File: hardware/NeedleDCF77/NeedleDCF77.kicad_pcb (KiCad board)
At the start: 2 copper layers, 3 parts, among them J1 USB_C_Receptacle_USB2.0, U1 LTC3558, U2 STM32L051C8Tx

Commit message: Import changes to PCB
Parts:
- added C1: 100nF, Capacitor_SMD:C_0805_2012Metric_Pad1.18x1.45mm_HandSolder, F.Cu at (233.5, 96.0)
- added C10: 22pF, Capacitor_SMD:C_0805_2012Metric_Pad1.18x1.45mm_HandSolder, F.Cu at (233.5, 108.0)
- added C11: 22pF, Capacitor_SMD:C_0805_2012Metric_Pad1.18x1.45mm_HandSolder, F.Cu at (238.3, 96.0)
- added C12: 10pF, Capacitor_SMD:C_0805_2012Metric_Pad1.18x1.45mm_HandSolder, F.Cu at (238.3, 99.0)
- added C13: 10pF, Capacitor_SMD:C_0805_2012Metric_Pad1.18x1.45mm_HandSolder, F.Cu at (238.3, 102.0)
- added C14: 10uF, Capacitor_Tantalum_SMD:CP_EIA-3216-18_Kemet-A_Pad1.58x1.35mm_HandSolder, F.Cu at (195.7, 111.4)
- added C15: 10pF, Capacitor_SMD:C_0805_2012Metric_Pad1.18x1.45mm_HandSolder, F.Cu at (238.3, 105.0)
- added C16: 4.7uF, Capacitor_SMD:CP_Elec_4x5.7, F.Cu at (249.4, 97.4)
- added C17: 10pF, Capacitor_SMD:C_0805_2012Metric_Pad1.18x1.45mm_HandSolder, F.Cu at (238.3, 108.0)
- added C18: 10pF, Capacitor_SMD:C_0805_2012Metric_Pad1.18x1.45mm_HandSolder, F.Cu at (243.1, 96.0)
- added C19: 100nF, Capacitor_SMD:C_0805_2012Metric_Pad1.18x1.45mm_HandSolder, F.Cu at (243.1, 99.0)
- added C2: 10uF, Capacitor_SMD:C_1206_3216Metric_Pad1.33x1.80mm_HandSolder, F.Cu at (251.4, 88.3)
- added C20: 4.7uF, Capacitor_Tantalum_SMD:CP_EIA-3528-21_Kemet-B_Pad1.50x2.35mm_HandSolder, F.Cu at (195.9, 115.1)
- added C21: 4.7uF, Capacitor_SMD:CP_Elec_4x5.7, F.Cu at (249.4, 103.3)
- added C22: 4.7uF, Capacitor_SMD:CP_Elec_4x5.7, F.Cu at (249.4, 109.1)
- added C23: 1uF, Capacitor_SMD:C_0805_2012Metric_Pad1.18x1.45mm_HandSolder, F.Cu at (243.1, 102.0)
- added C24: 100nF, Capacitor_SMD:C_0805_2012Metric_Pad1.18x1.45mm_HandSolder, F.Cu at (243.1, 105.0)
- added C3: 0.22uF, Capacitor_SMD:C_1206_3216Metric_Pad1.33x1.80mm_HandSolder, F.Cu at (251.4, 91.7)
- added C4: 10uF, Capacitor_Tantalum_SMD:CP_EIA-3216-18_Kemet-A_Pad1.58x1.35mm_HandSolder, F.Cu at (195.7, 101.9)
- added C5: 100nF, Capacitor_SMD:C_0805_2012Metric_Pad1.18x1.45mm_HandSolder, F.Cu at (233.5, 99.0)
- added C6: 100nF, Capacitor_SMD:C_0805_2012Metric_Pad1.18x1.45mm_HandSolder, F.Cu at (233.5, 102.0)
- added C7: 10uF, Capacitor_Tantalum_SMD:CP_EIA-3216-18_Kemet-A_Pad1.58x1.35mm_HandSolder, F.Cu at (195.7, 105.1)
- added C8: 10pF, Capacitor_SMD:C_0805_2012Metric_Pad1.18x1.45mm_HandSolder, F.Cu at (233.5, 105.0)
- added C9: 10uF, Capacitor_Tantalum_SMD:CP_EIA-3216-18_Kemet-A_Pad1.58x1.35mm_HandSolder, F.Cu at (195.7, 108.2)
- added D1: SSL14, Diode_SMD:D_SMA_Handsoldering, F.Cu at (241.9, 80.4)
- added D2: BZV55B5V6, Diode_SMD:D_MiniMELF, F.Cu at (240.2, 117.7)
- added D3: CD4148W, Diode_SMD:D_0805_2012Metric, F.Cu at (228.3, 115.2)
- added D4: 6.2V, Diode_THT:D_DO-35_SOD27_P2.54mm_Vertical_AnodeUp, F.Cu at (238.8, 84.5)
- added F1: 2A, Fuse:Fuse_2512_6332Metric_Pad1.52x3.35mm_HandSolder, F.Cu at (250.0, 114.5)
- added J2: Battery, Connector_Molex:Molex_KK-254_AE-6410-03A_1x03_P2.54mm_Vertical, F.Cu at (229.5, 82.0)
- added J3: DSW, Connector_PinHeader_2.54mm:PinHeader_1x04_P2.54mm_Vertical, F.Cu at (255.6, 96.8)
- added J4: UART, Connector_PinHeader_2.54mm:PinHeader_1x03_P2.54mm_Vertical, F.Cu at (217.6, 106.7)
- added J5: Hours, Connector_Molex:Molex_KK-254_AE-6410-02A_1x02_P2.54mm_Vertical, F.Cu at (222.2, 90.6)
- added J6: Minutes, Connector_Molex:Molex_KK-254_AE-6410-02A_1x02_P2.54mm_Vertical, F.Cu at (229.3, 90.6)
- added J7: Seconds, Connector_Molex:Molex_KK-254_AE-6410-02A_1x02_P2.54mm_Vertical, F.Cu at (236.5, 90.6)
- added JP1: ~, Jumper:SolderJumper-2_P1.3mm_Open_TrianglePad1.0x1.5mm, F.Cu at (245.1, 84.4)
- added L1: 15uH, Inductor_SMD:L_12x12mm_H8mm, F.Cu at (193.5, 79.0)
- added L2: 15uH, Inductor_SMD:L_12x12mm_H8mm, F.Cu at (193.5, 93.2)
- added L3: 4.7uH, Inductor_SMD:L_Ferrocore_DLG-0504, F.Cu at (252.4, 75.4)
- added L4: 2.2uH, Inductor_SMD:L_Ferrocore_DLG-0504, F.Cu at (252.4, 82.4)
- added R1: 5k1, Resistor_SMD:R_0805_2012Metric_Pad1.20x1.40mm_HandSolder, F.Cu at (203.3, 88.1)
- added R10: 120k, Resistor_SMD:R_1206_3216Metric_Pad1.30x1.75mm_HandSolder, F.Cu at (234.0, 111.2)
- added R11: 300k, Resistor_SMD:R_0805_2012Metric_Pad1.20x1.40mm_HandSolder, F.Cu at (208.0, 97.0)
- added R12: 1, Resistor_SMD:R_0805_2012Metric_Pad1.20x1.40mm_HandSolder, F.Cu at (208.0, 99.9)
- added R13: 820k, Resistor_SMD:R_0805_2012Metric_Pad1.20x1.40mm_HandSolder, F.Cu at (208.0, 102.9)
- added R14: 62k, Resistor_THT:R_Axial_DIN0207_L6.3mm_D2.5mm_P2.54mm_Vertical, F.Cu at (221.9, 115.7)
- added R15: 15k, Resistor_SMD:R_0805_2012Metric_Pad1.20x1.40mm_HandSolder, F.Cu at (212.8, 88.1)
- added R16: 390k, Resistor_SMD:R_0805_2012Metric_Pad1.20x1.40mm_HandSolder, F.Cu at (212.8, 91.1)
- added R17: 10k, Resistor_SMD:R_0805_2012Metric_Pad1.20x1.40mm_HandSolder, F.Cu at (212.8, 94.0)
- added R18: 10k, Resistor_SMD:R_0805_2012Metric_Pad1.20x1.40mm_HandSolder, F.Cu at (212.8, 97.0)
- added R19: 22k, Resistor_SMD:R_0805_2012Metric_Pad1.20x1.40mm_HandSolder, F.Cu at (212.8, 99.9)
- added R2: 5k1, Resistor_SMD:R_0805_2012Metric_Pad1.20x1.40mm_HandSolder, F.Cu at (203.3, 91.1)
- added R20: R_Small, Resistor_SMD:R_0805_2012Metric_Pad1.20x1.40mm_HandSolder, F.Cu at (212.8, 102.9)
- added R21: R_Small, Resistor_SMD:R_0805_2012Metric_Pad1.20x1.40mm_HandSolder, F.Cu at (217.5, 88.1)
- added R22: R_Small, Resistor_SMD:R_0805_2012Metric_Pad1.20x1.40mm_HandSolder, F.Cu at (217.5, 91.1)
- added R23: 51k, Resistor_SMD:R_0603_1608Metric_Pad0.98x0.95mm_HandSolder, F.Cu at (228.2, 118.0)
- added R24: 3R9, Resistor_SMD:R_1206_3216Metric_Pad1.30x1.75mm_HandSolder, F.Cu at (234.0, 114.5)
- added R25: 470, Resistor_SMD:R_0805_2012Metric_Pad1.20x1.40mm_HandSolder, F.Cu at (217.5, 94.0)
- added R26: 470, Resistor_SMD:R_0805_2012Metric_Pad1.20x1.40mm_HandSolder, F.Cu at (217.5, 97.0)
- added R27: 3R9, Resistor_SMD:R_1206_3216Metric_Pad1.30x1.75mm_HandSolder, F.Cu at (234.0, 117.8)
- added R3: Rntc, Resistor_SMD:R_0805_2012Metric_Pad1.20x1.40mm_HandSolder, F.Cu at (203.3, 94.0)
- added R4: 100k, Resistor_SMD:R_0805_2012Metric_Pad1.20x1.40mm_HandSolder, F.Cu at (203.3, 97.0)
- added R5: 820k, Resistor_SMD:R_0805_2012Metric_Pad1.20x1.40mm_HandSolder, F.Cu at (203.3, 99.9)
- added R6: 1k8, Resistor_SMD:R_0805_2012Metric_Pad1.20x1.40mm_HandSolder, F.Cu at (203.3, 102.9)
- added R7: 300k, Resistor_SMD:R_0805_2012Metric_Pad1.20x1.40mm_HandSolder, F.Cu at (208.0, 88.1)
- added R8: 100k, Resistor_SMD:R_0805_2012Metric_Pad1.20x1.40mm_HandSolder, F.Cu at (208.0, 91.1)
- added R9: 1k, Resistor_SMD:R_0805_2012Metric_Pad1.20x1.40mm_HandSolder, F.Cu at (208.0, 94.0)
- added RV1: Hour_pot, Potentiometer_THT:Potentiometer_Bourns_3296Y_Vertical, F.Cu at (228.0, 96.4)
- added RV2: Minutes_pot, Potentiometer_THT:Potentiometer_Bourns_3296Y_Vertical, F.Cu at (228.0, 102.8)
- added RV3: Second_pot, Potentiometer_THT:Potentiometer_Bourns_3296Y_Vertical, F.Cu at (228.0, 109.2)
- added SW1: ShowDate, Connector_Molex:Molex_KK-254_AE-6410-02A_1x02_P2.54mm_Vertical, F.Cu at (243.6, 90.6)
- added U3: MAS6180_77kHz, DCF77_module:MAS6180_module, F.Cu at (201.7, 72.6)
- added U4: LT1617, Package_TO_SOT_SMD:SOT-23-5_HandSoldering, F.Cu at (189.0, 115.8)
- added U5: PT6312, Package_QFP:LQFP-44_10x10mm_P0.8mm, F.Cu at (208.1, 111.5)
- added U6: LM4871, Package_SO:SOIC-8_3.9x4.9mm_P1.27mm, F.Cu at (241.2, 112.8)
- added VFD1: FG95A, VFD:FG95A, F.Cu at (194.3, 70.1)
- added Y1: 8MHz, Crystal:Crystal_SMD_HC49-SD_HandSoldering, F.Cu at (237.9, 75.0)
- added Y2: 32.768kHz, Crystal:Crystal_C38-LF_D3.0mm_L8.0mm_Horizontal_1EP_style2, F.Cu at (188.5, 101.7)
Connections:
- J1 pad A1: Net-(J1-PadA1) -> GND
- J1 pad A12: Net-(J1-PadA1) -> GND
- J1 pad A5: unconnected-(J1-PadA5) -> Net-(J1-CC1)
- J1 pad B1: Net-(J1-PadA1) -> GND
- J1 pad B12: Net-(J1-PadA1) -> GND
- J1 pad B5: unconnected-(J1-PadB5) -> Net-(J1-CC2)
- J1 pad S1: unconnected-(J1-PadS1) -> GND
- U1 pad 1: unconnected-(U1-Pad1) -> GND
- U1 pad 10: unconnected-(U1-Pad10) -> Net-(U1-SWCD2)
- U1 pad 11: unconnected-(U1-Pad11) -> +5VD
- U1 pad 12: unconnected-(U1-Pad12) -> LTC_SUSP
- U1 pad 13: unconnected-(U1-Pad13) -> Net-(U1-FB2)
- U1 pad 14: unconnected-(U1-Pad14) -> Net-(U1-Vc2)
- U1 pad 15: unconnected-(U1-Pad15) -> Net-(U1-EN2)
- U1 pad 16: unconnected-(U1-Pad16) -> LTC_HPWR
- U1 pad 17: unconnected-(U1-Pad17) -> NTC
- U1 pad 18: unconnected-(U1-Pad18) -> Net-(U1-PROG)
- U1 pad 19: unconnected-(U1-Pad19) -> LTC_CHRG
- U1 pad 2: unconnected-(U1-Pad2) -> VBAT
- U1 pad 20: unconnected-(U1-Pad20) -> VBUS_P
- U1 pad 21: unconnected-(U1-Pad21) -> GND
- U1 pad 3: unconnected-(U1-Pad3) -> LTC_MODE
- U1 pad 4: unconnected-(U1-Pad4) -> Net-(U1-FB1)
- U1 pad 5: unconnected-(U1-Pad5) -> Net-(U1-EN1)
- U1 pad 6: unconnected-(U1-Pad6) -> Net-(U1-SW1)
- U1 pad 7: unconnected-(U1-Pad7) -> VBAT
- U1 pad 8: unconnected-(U1-Pad8) -> VBAT
- U1 pad 9: unconnected-(U1-Pad9) -> Net-(U1-SWAB2)
- U2 pad 10: unconnected-(U2-Pad10) -> GPIO_EXTI0
- U2 pad 11: unconnected-(U2-Pad11) -> PWM_Min
- U2 pad 12: unconnected-(U2-Pad12) -> PWM_Hour
- U2 pad 13: unconnected-(U2-Pad13) -> PWM_Sec
- U2 pad 14: unconnected-(U2-Pad14) -> SPI1_NSS
- U2 pad 15: unconnected-(U2-Pad15) -> PWM_Fosc
- U2 pad 16: unconnected-(U2-Pad16) -> DCF77_TIME
- U2 pad 21: unconnected-(U2-Pad21) -> DCF77_PDN
- U2 pad 22: unconnected-(U2-Pad22) -> ~{SHDN_-24V}
- U2 pad 23: unconnected-(U2-Pad23) -> GND
- U2 pad 24: unconnected-(U2-Pad24) -> +3V0
- U2 pad 25: unconnected-(U2-Pad25) -> LTC_SUSP
- U2 pad 26: unconnected-(U2-Pad26) -> LTC_HPWR
- U2 pad 27: unconnected-(U2-Pad27) -> LTC_MODE
- U2 pad 28: unconnected-(U2-Pad28) -> LTC_CHRG
- U2 pad 3: unconnected-(U2-Pad3) -> Net-(U2-PC14)
- U2 pad 30: unconnected-(U2-Pad30) -> USART1_TX
- U2 pad 31: unconnected-(U2-Pad31) -> USART1_RX
- U2 pad 34: unconnected-(U2-Pad34) -> SWDIO
- U2 pad 35: unconnected-(U2-Pad35) -> GND
- U2 pad 36: unconnected-(U2-Pad36) -> +3V0
- U2 pad 37: unconnected-(U2-Pad37) -> SWCLK
- U2 pad 39: unconnected-(U2-Pad39) -> SPI1_SCK
- U2 pad 4: unconnected-(U2-Pad4) -> Net-(U2-PC15)
- U2 pad 40: unconnected-(U2-Pad40) -> SPI1_MISO
- U2 pad 41: unconnected-(U2-Pad41) -> SPI1_MOSI
- U2 pad 47: unconnected-(U2-Pad47) -> GND
- U2 pad 48: unconnected-(U2-Pad48) -> +3V0
- U2 pad 5: unconnected-(U2-Pad5) -> Net-(U2-PH0)
- U2 pad 6: unconnected-(U2-Pad6) -> Net-(U2-PH1)
- U2 pad 7: unconnected-(U2-Pad7) -> Net-(U2-NRST)
- U2 pad 8: unconnected-(U2-Pad8) -> GND
- U2 pad 9: unconnected-(U2-Pad9) -> +3V0

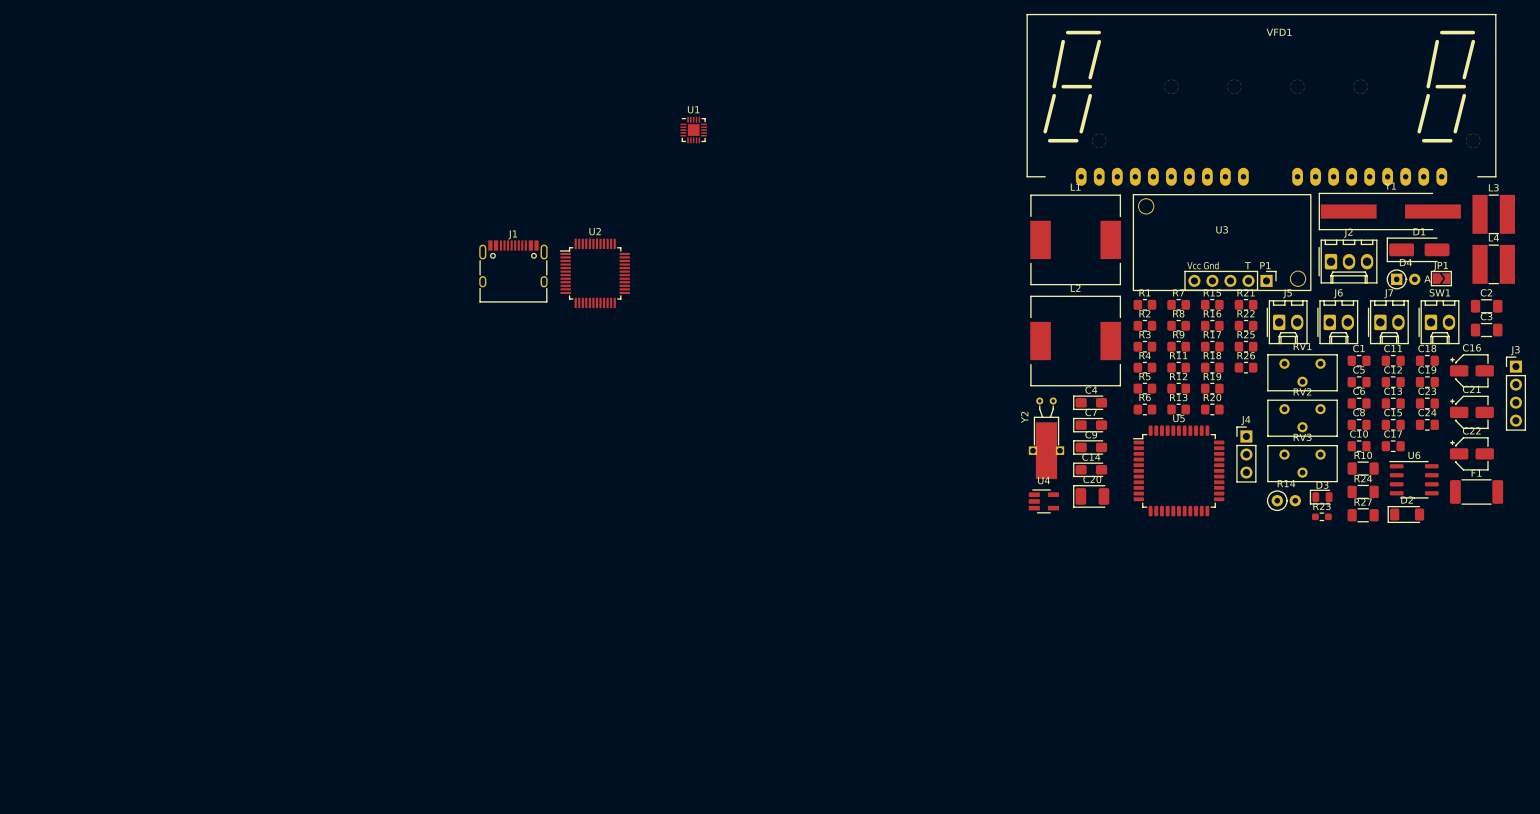
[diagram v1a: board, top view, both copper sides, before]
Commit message: Add battery measurement circuit and generate ADC code
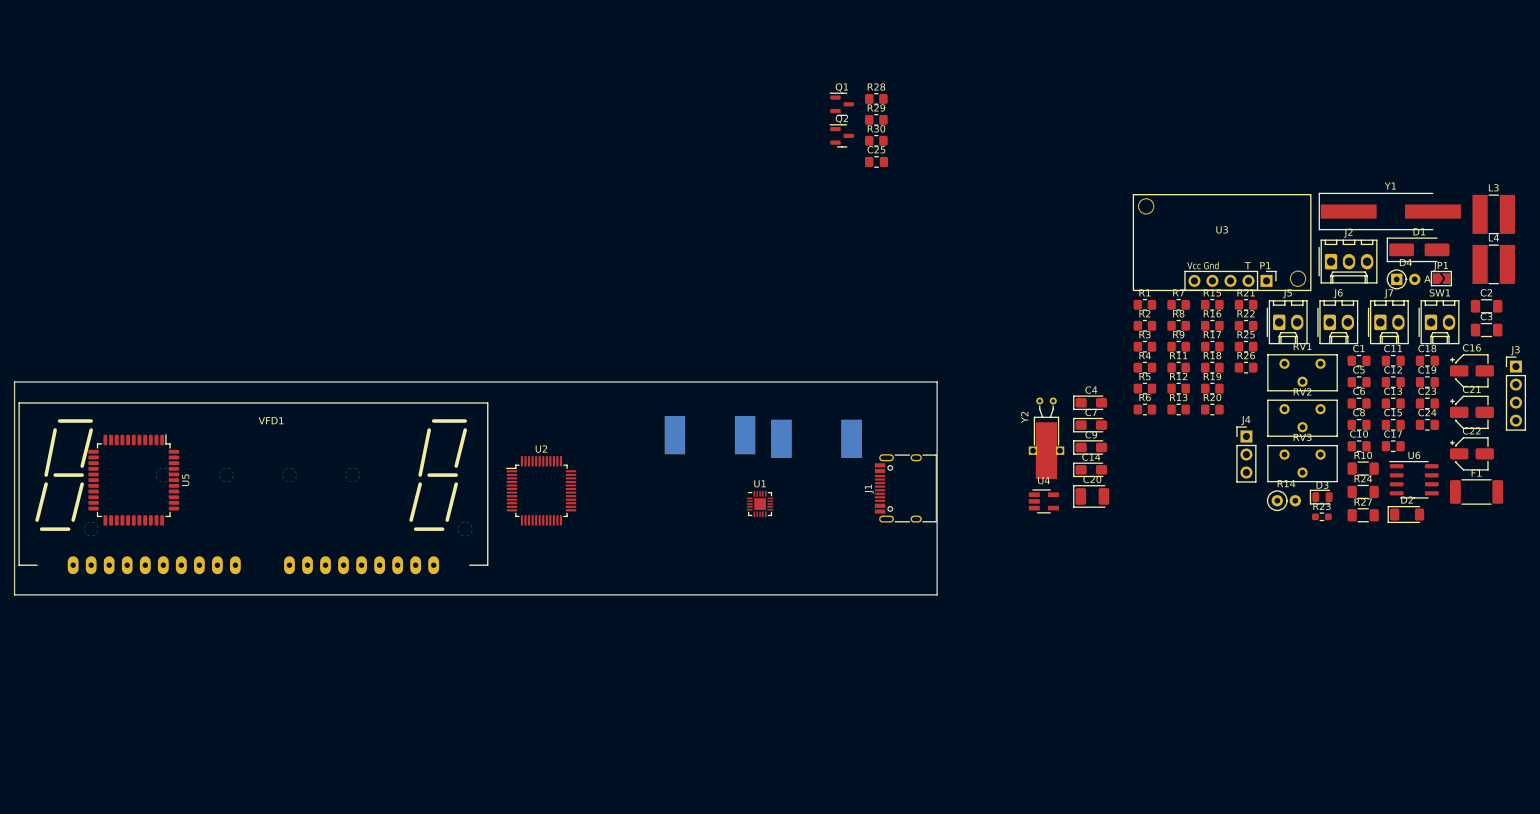
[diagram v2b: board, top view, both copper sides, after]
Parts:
- added C25: 10pF, Capacitor_SMD:C_0805_2012Metric_Pad1.18x1.45mm_HandSolder, F.Cu at (165.5, 68.0)
- added Q1: AO3401A, Package_TO_SOT_SMD:SOT-23, F.Cu at (160.6, 59.9)
- added Q2: AO3400A, Package_TO_SOT_SMD:SOT-23, F.Cu at (160.6, 64.3)
- added R28: 100k, Resistor_SMD:R_0805_2012Metric_Pad1.20x1.40mm_HandSolder, F.Cu at (165.4, 59.1)
- added R29: 22k, Resistor_SMD:R_0805_2012Metric_Pad1.20x1.40mm_HandSolder, F.Cu at (165.4, 62.1)
- added R30: 22k, Resistor_SMD:R_0805_2012Metric_Pad1.20x1.40mm_HandSolder, F.Cu at (165.4, 65.0)
- L1, L2: moved to B.Cu
- moved VFD1 152.2 mm to (52.3, 124.8)
- moved U5 147.3 mm to (60.8, 112.8), turned to -90 degrees
- moved J1 63.4 mm to (170.0, 114.0), turned to 90 degrees
- moved L1 58.4 mm to (142.0, 106.5), turned to 180 degrees
- moved U1 53.5 mm to (149.1, 116.2)
- moved L2 39.0 mm to (157.0, 107.0), turned to 180 degrees
- moved U2 31.6 mm to (118.2, 114.3)
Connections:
- U2 pad 17: unconnected-(U2-PA7-Pad17) -> BATT_LEVEL
- U2 pad 29: unconnected-(U2-PA8-Pad29) -> BATT_CHECK
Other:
- board outline added: 130 x 30 mm

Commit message: Bulk work - working on layout
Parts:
- C21, C22, J2, J3, J4, J5, J6, J7, L3, L4, SW1, Y1: moved to B.Cu
- R20: value R_Small -> 22k
- R21, R22: value R_Small -> 51k; footprint Resistor_SMD:R_0805_2012Metric_Pad1.20x1.40mm_HandSolder -> Resistor_SMD:R_0603_1608Metric_Pad0.98x0.95mm_HandSolder
- RV1: value Hour_pot -> 10k; moved to B.Cu
- RV2: value Minutes_pot -> 10k; moved to B.Cu
- RV3: value Second_pot -> 10k; moved to B.Cu
- moved C23 195.6 mm to (47.5, 104.4), turned to 90 degrees
- moved C22 194.3 mm to (55.2, 102.4)
- moved C21 194.2 mm to (55.2, 107.4)
- moved U6 188.4 mm to (53.0, 104.9)
- moved R24 182.6 mm to (51.5, 120.5), turned to -90 degrees
- moved C24 175.9 mm to (68.0, 121.5)
- moved D4 175.6 mm to (64.0, 101.4), turned to -90 degrees
- moved J4 171.2 mm to (52.5, 152.0), turned to 180 degrees
- moved C3 168.3 mm to (83.4, 102.0), turned to 180 degrees
- moved D1 167.3 mm to (76.0, 102.0)
- moved C2 164.9 mm to (87.5, 106.5), turned to -90 degrees
- moved R25 158.0 mm to (60.0, 106.9), turned to 90 degrees
- moved R26 157.6 mm to (60.0, 102.9), turned to -90 degrees
- moved R23 149.5 mm to (79.0, 108.5), turned to 180 degrees
- moved R27 142.3 mm to (92.5, 132.5)
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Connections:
- U2 pad 32: unconnected-(U2-PA11-Pad32) -> LTC_EN2
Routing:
- net GND: track 0.00 -> 8.65 mm
- net +5VD: track 0.00 -> 7.42 mm
- net Net-(U1-SWCD2): track 0.00 -> 7.00 mm, vias 0 -> 1
- net Net-(U6-+IN): track 0.00 -> 4.34 mm
- net Net-(C22-Pad2): track 0.00 -> 3.21 mm, vias 0 -> 1
- net Net-(C21-Pad2): track 0.00 -> 3.21 mm, vias 0 -> 1
- net Net-(U1-FB2): track 0.00 -> 2.97 mm
- net Net-(U1-EN2): track 0.00 -> 2.72 mm
- net Net-(U1-EN1): track 0.00 -> 2.46 mm
- net VBAT: track 0.00 -> 2.37 mm, vias 0 -> 1
- net Net-(U6-VO2): track 0.00 -> 2.32 mm, vias 0 -> 1
- net Net-(U6-VO1): track 0.00 -> 2.32 mm, vias 0 -> 1
- net Net-(U1-SWAB2): track 0.00 -> 2.21 mm, vias 0 -> 1
- net Net-(D4-K): track 0.00 -> 2.00 mm
- net Net-(U1-SW1): track 0.00 -> 1.32 mm, vias 0 -> 1

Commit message: Use HSI instead of HSE
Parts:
- removed C10, C11: 22pF, Capacitor_SMD:C_0805_2012Metric_Pad1.18x1.45mm_HandSolder
- removed Y1: 8MHz, Crystal:Crystal_SMD_HC49-SD_HandSoldering
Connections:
- U2 pad 5: Net-(U2-PH0) -> unconnected-(U2-PH0-Pad5)
- U2 pad 6: Net-(U2-PH1) -> unconnected-(U2-PH1-Pad6)

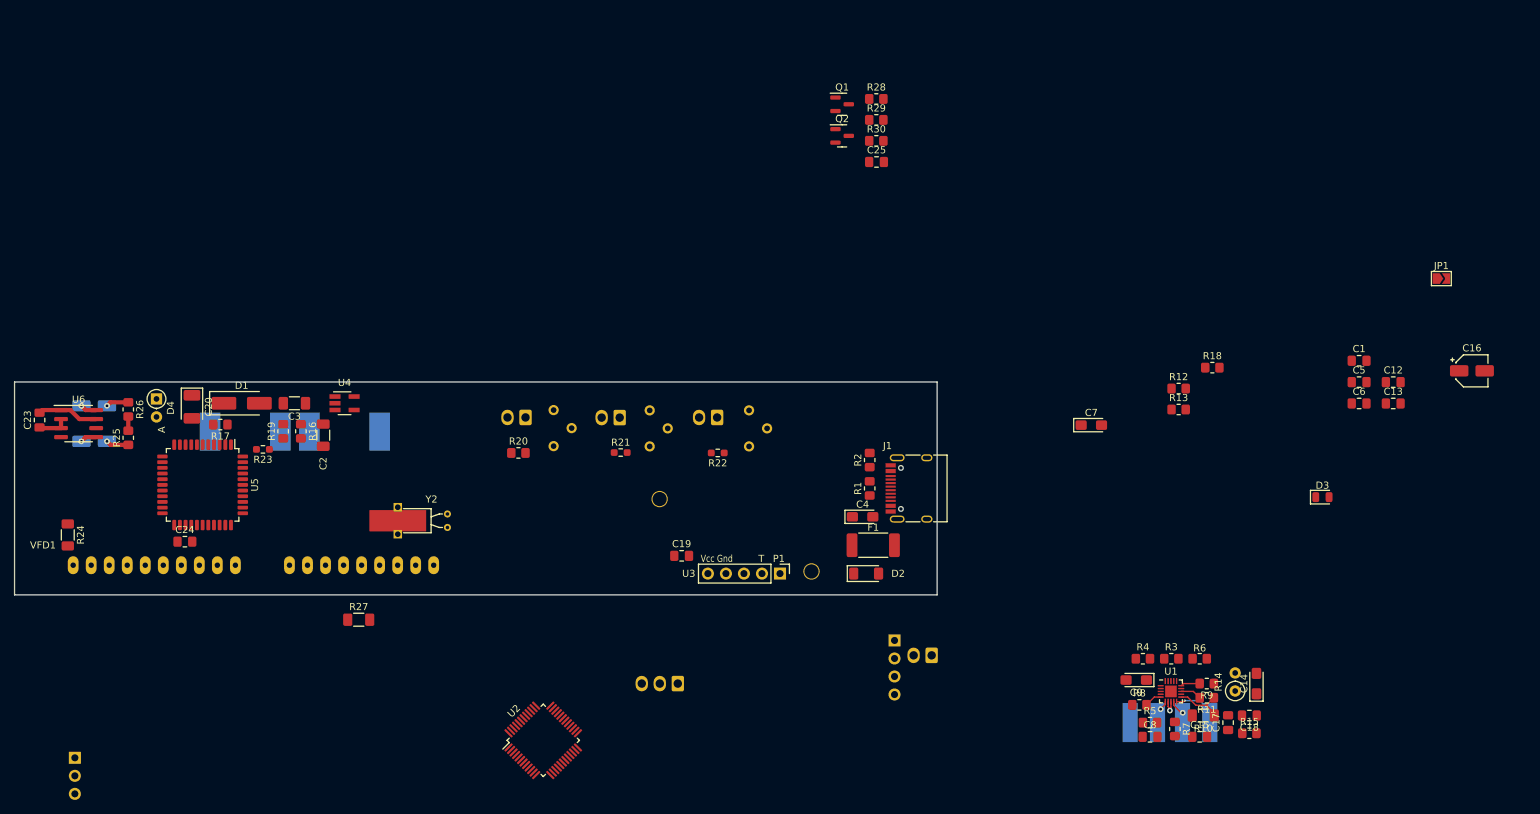
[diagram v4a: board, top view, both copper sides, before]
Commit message: Initial version of PCB placement and routing
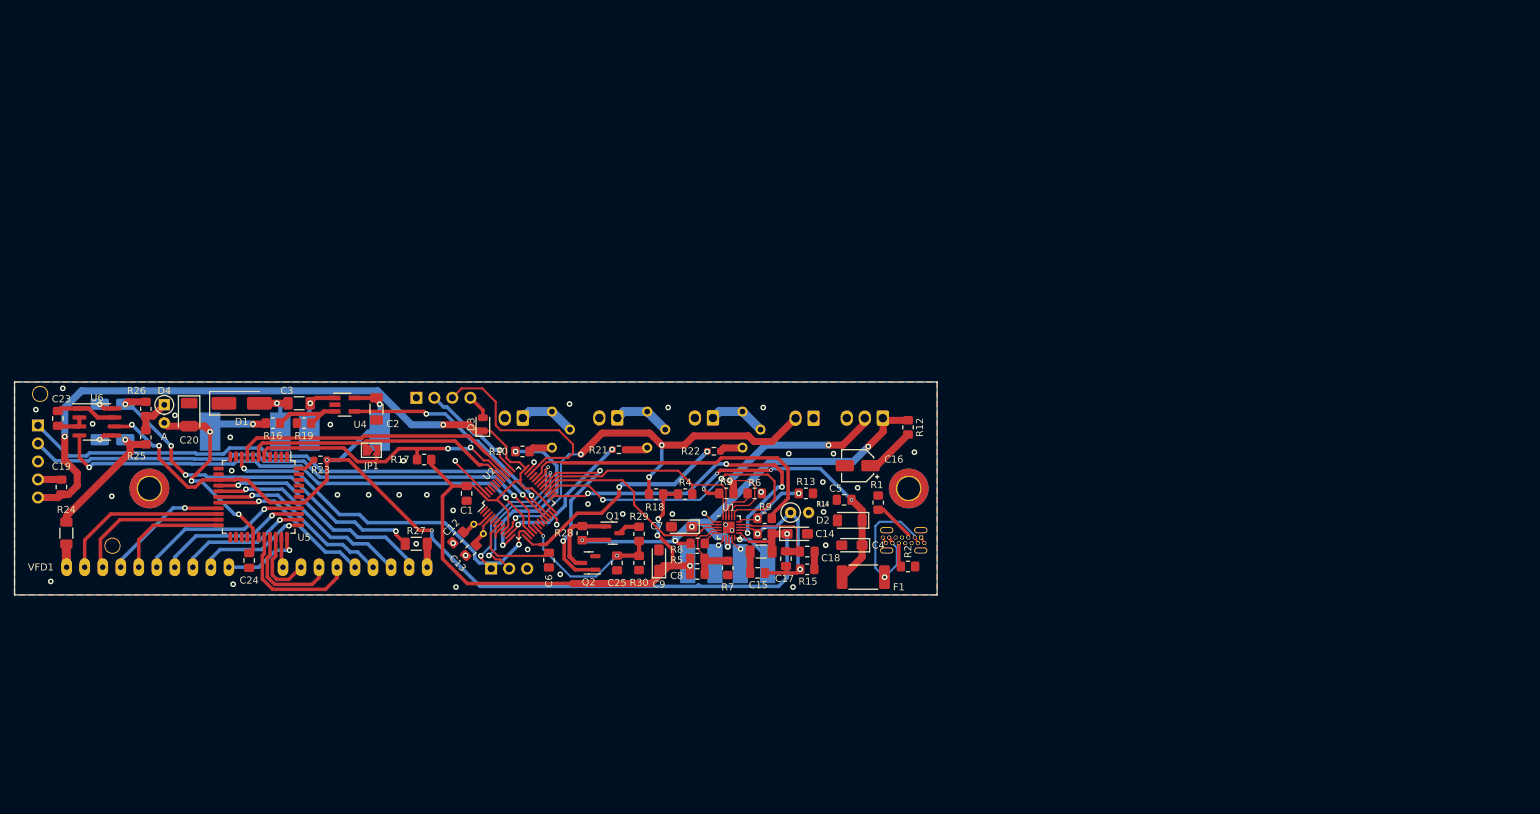
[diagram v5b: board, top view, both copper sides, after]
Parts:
- added H1: Hole, MountingHole:MountingHole_3.2mm_M3_DIN965_Pad_TopBottom, F.Cu at (170.0, 114.0)
- added H2: Hole, MountingHole:MountingHole_3.2mm_M3_DIN965_Pad_TopBottom, F.Cu at (63.0, 114.0)
- J1: footprint Connector_USB:USB_C_Receptacle_HRO_TYPE-C-31-M-12 -> Molex USB C:Molex-2169890001-MFG; moved to B.Cu
- U3: moved to B.Cu
- Y2: footprint Crystal:Crystal_C38-LF_D3.0mm_L8.0mm_Horizontal_1EP_style2 -> Crystal:Crystal_C38-LF_D3.0mm_L8.0mm_Horizontal; moved to B.Cu
- moved JP1 152.7 mm to (94.3, 108.6)
- moved C12 133.6 mm to (106.5, 120.9), turned to 45 degrees
- moved C13 131.6 mm to (108.3, 122.7), turned to 45 degrees
- moved C1 127.1 mm to (107.7, 114.7), turned to -90 degrees
- moved D3 118.7 mm to (110.0, 105.0), turned to 90 degrees
- moved C6 116.3 mm to (119.3, 124.1), turned to 90 degrees
- moved C19 87.9 mm to (50.6, 113.8), turned to 90 degrees
- moved C16 87.6 mm to (162.8, 110.8), turned to 180 degrees
- moved R18 80.4 mm to (134.4, 114.8), turned to 180 degrees
- moved J3 75.6 mm to (100.6, 101.2), turned to -90 degrees
- moved C5 74.4 mm to (160.9, 115.6)
- moved U3 74.3 mm to (59.5, 123.9), turned to 90 degrees
- moved R28 73.9 mm to (124.0, 120.3), turned to -90 degrees
- moved Q2 70.0 mm to (124.9, 124.5), turned to 180 degrees
- moved C9 69.4 mm to (134.8, 124.1), turned to 90 degrees
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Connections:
- Y2 pad 1: Net-(U2-PC15) -> Net-(U2-PC14)
- Y2 pad 2: Net-(U2-PC14) -> Net-(U2-PC15)
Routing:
- net +3V0: track 0.00 -> 185.7 mm, vias 0 -> 5
- net +5VD: track 7.42 -> 147.5 mm, vias 0 -> 6
- net DCF77_PDN: track 0.00 -> 78.0 mm, vias 0 -> 1
- net DCF77_TIME: track 0.00 -> 76.9 mm, vias 0 -> 1
- net PWM_Fosc: track 0.00 -> 72.7 mm, vias 0 -> 2
- net VBAT: track 2.37 -> 72.9 mm, vias 1 -> 5
- net GPIO_EXTI0: track 0.00 -> 60.5 mm, vias 0 -> 4
- net SPI1_NSS: track 0.00 -> 50.9 mm, vias 0 -> 2
- net Net-(C22-Pad2): track 3.21 -> 52.1 mm, vias 1 -> 4
- net LTC_SUSP: track 0.00 -> 46.8 mm, vias 0 -> 4
- net LTC_EN2: track 0.00 -> 45.8 mm
- net LTC_HPWR: track 0.00 -> 44.3 mm, vias 0 -> 2
- net VBUS_P: track 0.00 -> 42.8 mm, vias 0 -> 4
- net SPI1_MISO: track 0.00 -> 41.2 mm, vias 0 -> 2
- net SPI1_SCK: track 0.00 -> 40.7 mm
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- added copper zone on B.Cu, net GND
- added copper zone on F.Cu, net GND
